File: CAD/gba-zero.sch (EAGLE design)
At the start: 57 parts, among them J1 SWTCHCRFT_3.5JACK5-JACK-SMD, P1 50_PIN_CON, P3 LINK_CONNECTOR, Q1 BSS138, U1 APX803, U2 NC7WZ16, U3 74LVC2G02, U4 74LVC3G04, U5 LM4875, U6 RPI-ZEROSMD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

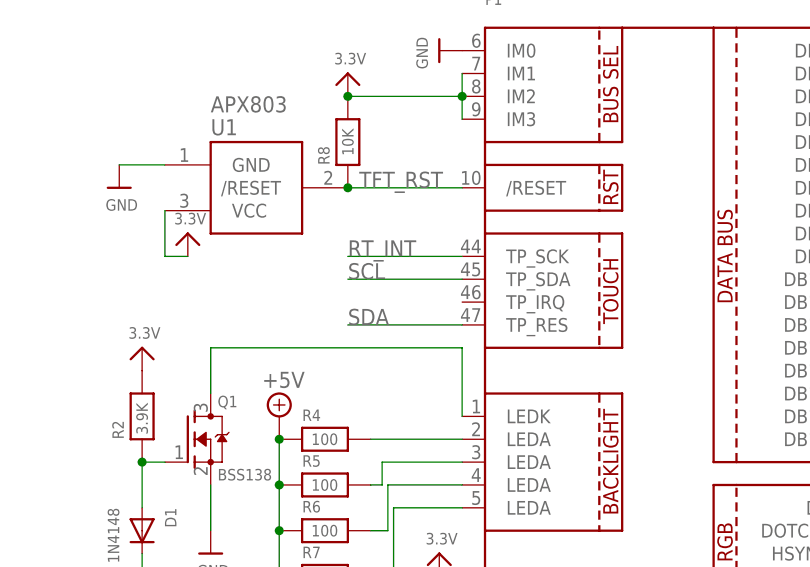
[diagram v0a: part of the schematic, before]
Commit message: Rerouted display control lines Added missing connection between pins 10 & 47 on the display connector
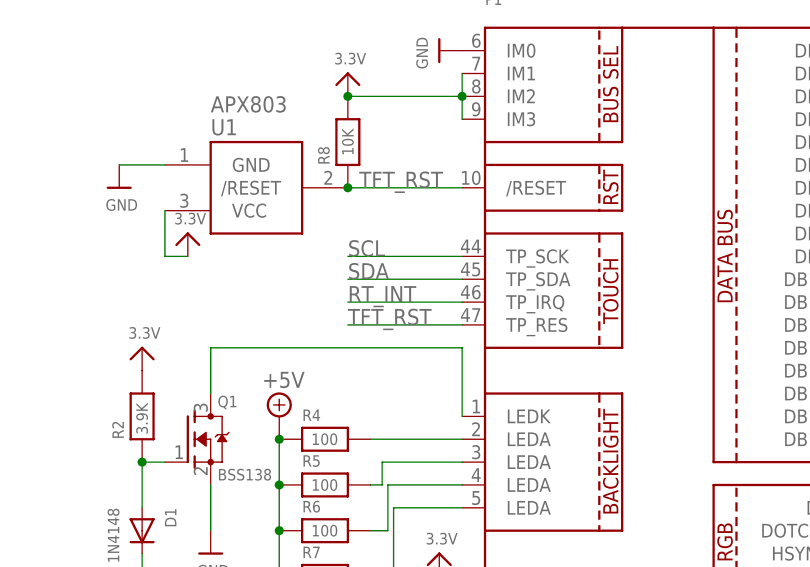
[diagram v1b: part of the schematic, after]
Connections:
- net RT_INT: now also P1.TP_IRQ; no longer P1.TP_SCK
- net SCL: now also P1.TP_SCK; no longer P1.TP_SDA
- net SDA: now also P1.TP_SDA; no longer P1.TP_RES
- net TFT_RST: now also P1.TP_RES
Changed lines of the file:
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@@
 <junction x="45.72" y="83.82"/>
+</segment>
+<segment>
+<wire x1="45.72" y1="68.58" x2="58.42" y2="68.58" width="0.1524" layer="91"/>
+<label x="45.72" y="68.58" size="1.778" layer="95"/>
+<pinref part="P1" gate="G$1" pin="TP_RES"/>
 </segment>
 </net>
@@
 </segment>
 <segment>
-<wire x1="58.42" y1="76.2" x2="45.72" y2="76.2" width="0.1524" layer="91"/>
-<pinref part="P1" gate="G$1" pin="TP_SCK"/>
-<label x="45.72" y="76.2" size="1.778" layer="95"/>
+<wire x1="58.42" y1="71.12" x2="45.72" y2="71.12" width="0.1524" layer="91"/>
+<label x="45.72" y="71.12" size="1.778" layer="95"/>
+<pinref part="P1" gate="G$1" pin="TP_IRQ"/>
 </segment>
 </net>
@@
 </segment>
 <segment>
-<pinref part="P1" gate="G$1" pin="TP_RES"/>
-<wire x1="58.42" y1="68.58" x2="45.72" y2="68.58" width="0.1524" layer="91"/>
-<label x="45.72" y="68.58" size="1.778" layer="95"/>
+<wire x1="58.42" y1="73.66" x2="45.72" y2="73.66" width="0.1524" layer="91"/>
+<label x="45.72" y="73.66" size="1.778" layer="95"/>
+<pinref part="P1" gate="G$1" pin="TP_SDA"/>
 </segment>
 </net>
@@
 </segment>
 <segment>
-<pinref part="P1" gate="G$1" pin="TP_SDA"/>
-<wire x1="58.42" y1="73.66" x2="45.72" y2="73.66" width="0.1524" layer="91"/>
-<label x="45.72" y="73.66" size="1.778" layer="95"/>
+<wire x1="58.42" y1="76.2" x2="45.72" y2="76.2" width="0.1524" layer="91"/>
+<label x="45.72" y="76.2" size="1.778" layer="95"/>
+<pinref part="P1" gate="G$1" pin="TP_SCK"/>
 </segment>
 </net>

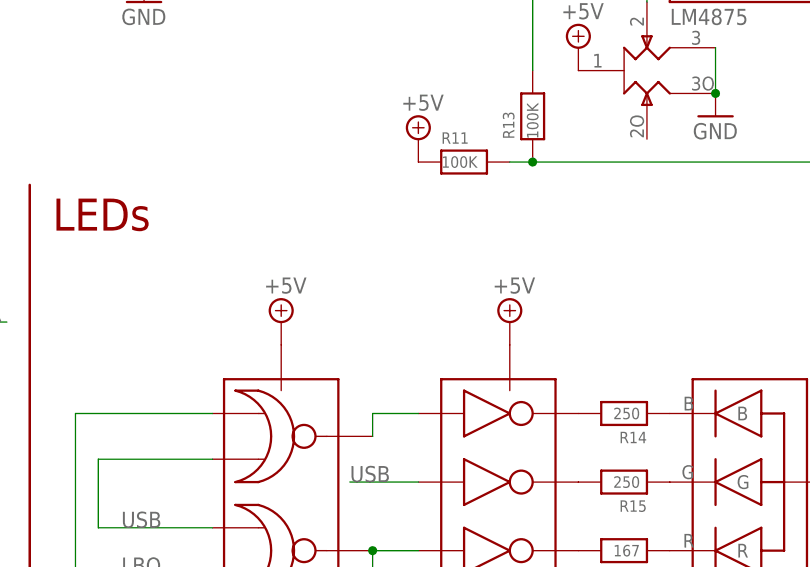
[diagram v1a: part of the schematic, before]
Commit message: Added diodes to power LED logic by USB & regulated 5V Cleaned up layout
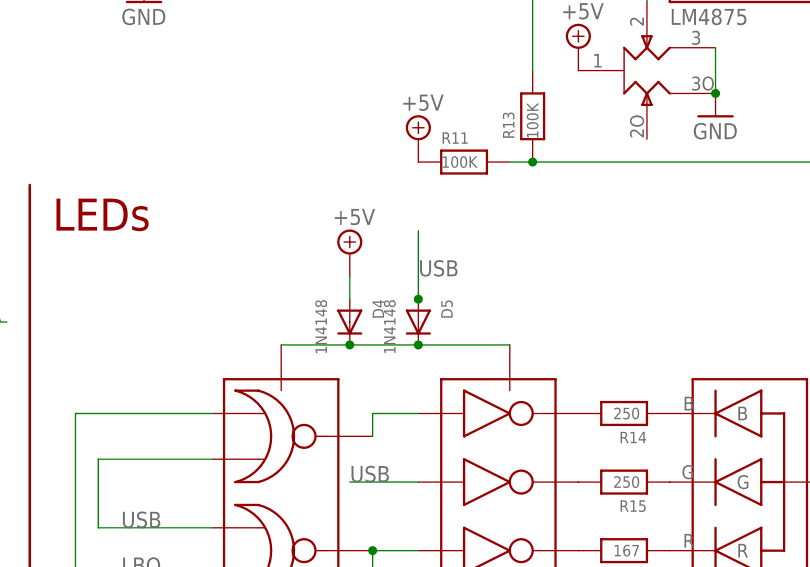
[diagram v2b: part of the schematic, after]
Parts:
- added D4, D5: 1N4148, microbuilder:DIODESOD-323
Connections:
- new net N$19: D4.C, D5.C, U3.VCC, U4.VCC
- net +5V: now also D4.A; no longer U3.VCC, U4.VCC
- net USB: now also D5.A
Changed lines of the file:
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@@
 <part name="D2" library="gba-zero-parts" deviceset="LTST-C19HE1WT" device=""/>
 <part name="SUPPLY2" library="supply2" deviceset="+5V" device=""/>
-<part name="SUPPLY5" library="supply2" deviceset="+5V" device=""/>
 <part name="SUPPLY9" library="supply2" deviceset="+5V" device=""/>
 <part name="GND7" library="microbuilder" deviceset="GND" device=""/>
@@
 <part name="R1" library="microbuilder" deviceset="RESISTOR" device="0603" value="0"/>
 <part name="R3" library="microbuilder" deviceset="RESISTOR" device="0603" value="0"/>
+<part name="D4" library="microbuilder" deviceset="DIODE" device="SOD-323" value="1N4148"/>
+<part name="D5" library="microbuilder" deviceset="DIODE" device="SOD-323" value="1N4148"/>
 </parts>
 <sheets>
@@
 <instance part="U4" gate="G$1" x="104.14" y="152.4"/>
 <instance part="D2" gate="G$1" x="129.54" y="152.4" rot="R180"/>
-<instance part="SUPPLY2" gate="+5V" x="78.74" y="170.18"/>
-<instance part="SUPPLY5" gate="+5V" x="104.14" y="170.18"/>
+<instance part="SUPPLY2" gate="+5V" x="86.36" y="177.8"/>
 <instance part="SUPPLY9" gate="+5V" x="139.7" y="154.94"/>
 <instance part="GND7" gate="G$1" x="78.74" y="132.08" rot="MR0"/>
@@
 <attribute name="VALUE" x="24.765" y="34.798" size="1.27" layer="96" font="vector" rot="R270"/>
 </instance>
+<instance part="D4" gate="G$1" x="86.36" y="170.18" rot="R270"/>
+<instance part="D5" gate="G$1" x="93.98" y="170.18" rot="R270"/>
 </instances>
 <busses>
@@
 <junction x="231.14" y="172.72"/>
 </segment>
+<segment>
+<wire x1="93.98" y1="172.72" x2="93.98" y2="180.34" width="0.1524" layer="91"/>
+<label x="93.98" y="175.26" size="1.778" layer="95"/>
+<pinref part="D5" gate="G$1" pin="A"/>
+<junction x="93.98" y="172.72"/>
+</segment>
 </net>
 <net name="LBO" class="0">
@@
 </segment>
 <segment>
-<pinref part="U3" gate="G$1" pin="VCC"/>
-<pinref part="SUPPLY2" gate="+5V" pin="+5V"/>
-</segment>
-<segment>
-<pinref part="U4" gate="G$1" pin="VCC"/>
-<pinref part="SUPPLY5" gate="+5V" pin="+5V"/>
-</segment>
-<segment>
 <pinref part="D2" gate="G$1" pin="VCC"/>
 <pinref part="SUPPLY9" gate="+5V" pin="+5V"/>
@@
 <pinref part="C9" gate="G$1" pin="P$1"/>
 <pinref part="SUPPLY8" gate="+5V" pin="+5V"/>
+</segment>
+<segment>
+<pinref part="D4" gate="G$1" pin="A"/>
+<pinref part="SUPPLY2" gate="+5V" pin="+5V"/>
+<wire x1="86.36" y1="175.26" x2="86.36" y2="172.72" width="0.1524" layer="91"/>
 </segment>
 </net>
@@
 </segment>
 </net>
+<net name="N$19" class="0">
+<segment>
+<pinref part="U3" gate="G$1" pin="VCC"/>
+<pinref part="U4" gate="G$1" pin="VCC"/>
+<wire x1="78.74" y1="167.64" x2="86.36" y2="167.64" width="0.1524" layer="91"/>
+<pinref part="D4" gate="G$1" pin="C"/>
+<wire x1="86.36" y1="167.64" x2="93.98" y2="167.64" width="0.1524" layer="91"/>
+<junction x="86.36" y="167.64"/>
+<pinref part="D5" gate="G$1" pin="C"/>
+<wire x1="93.98" y1="167.64" x2="104.14" y2="167.64" width="0.1524" layer="91"/>
+<junction x="93.98" y="167.64"/>
+</segment>
+</net>

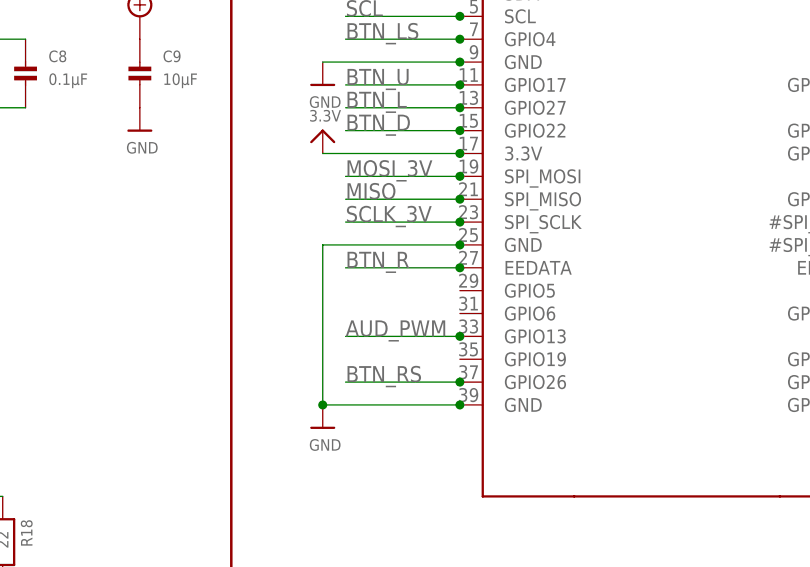
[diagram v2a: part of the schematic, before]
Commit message: Added LBO to a GPIO5
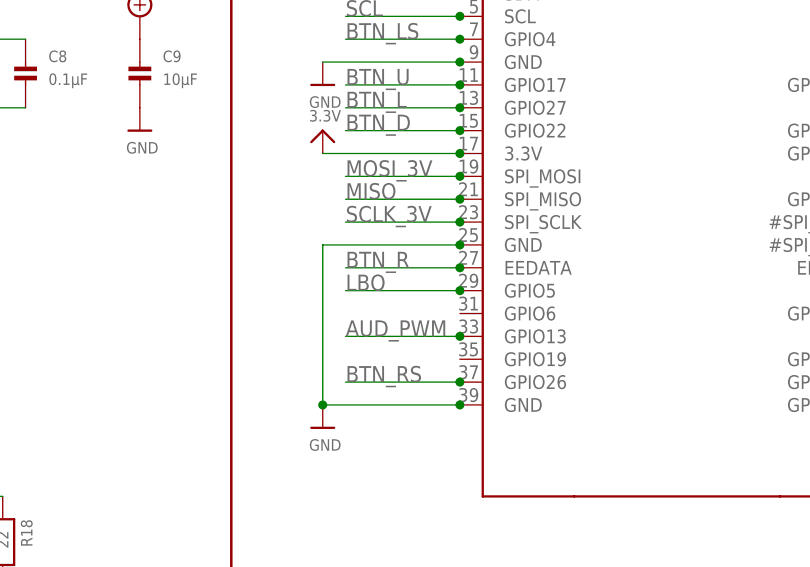
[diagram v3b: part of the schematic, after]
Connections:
- net LBO: now also U6.GPIO5
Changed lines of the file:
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@@
 <pinref part="U7" gate="G$1" pin="LBO"/>
+</segment>
+<segment>
+<wire x1="160.02" y1="60.96" x2="172.72" y2="60.96" width="0.1524" layer="91"/>
+<pinref part="U6" gate="G$1" pin="GPIO5"/>
+<junction x="172.72" y="60.96"/>
+<label x="160.02" y="60.96" size="1.778" layer="95"/>
 </segment>
 </net>

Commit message: Replaced 0805s with 0603s Fattened power traces
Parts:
- C11, C12, C14: device microbuilder:CAP_CERAMIC0805 -> microbuilder:CAP_CERAMIC0603
- R14, R15, R16, R18, R19, R2, R4, R5, R6, R7, R8: device microbuilder:RESISTOR0805 -> microbuilder:RESISTOR0603

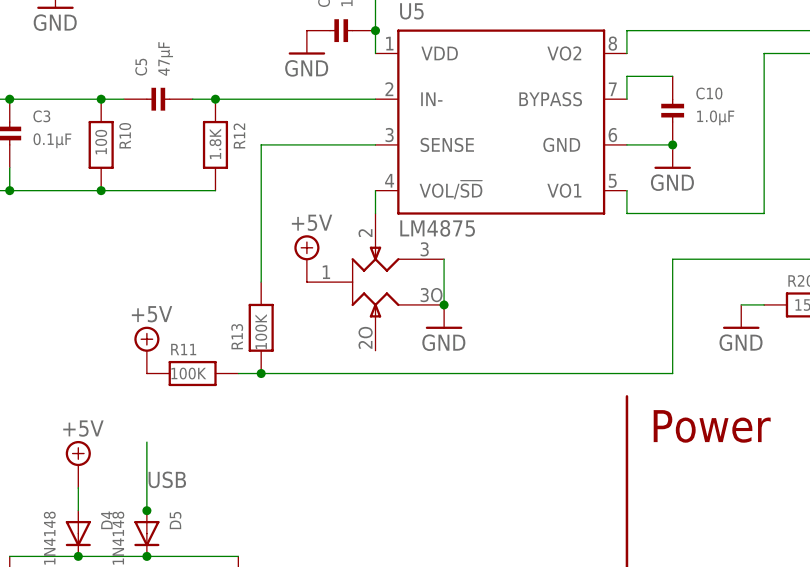
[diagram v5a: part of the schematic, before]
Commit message: Swapped VCC & GND for the volume dial
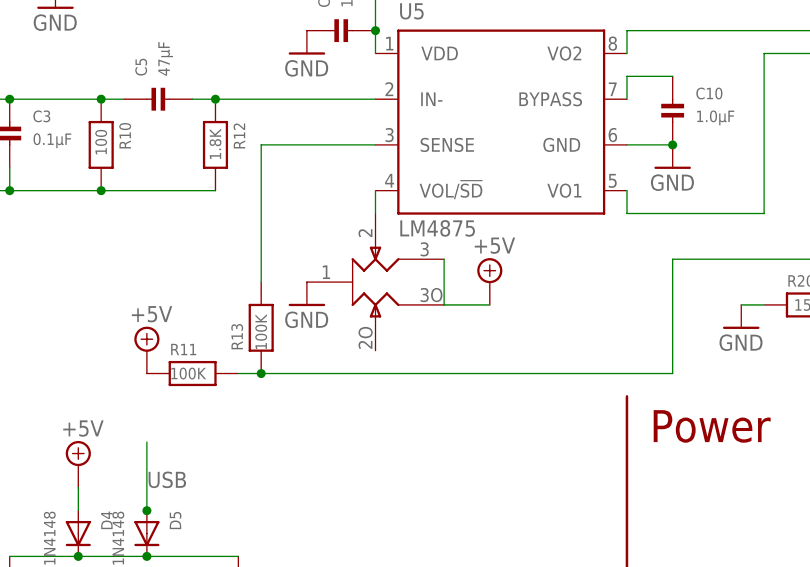
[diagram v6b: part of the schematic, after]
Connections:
- net +5V: now also R17.3, R17.3O; no longer R17.1
- net GND: now also R17.1; no longer R17.3, R17.3O
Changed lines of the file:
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@@
 <attribute name="VALUE" x="187.96" y="227.33" size="1.27" layer="96"/>
 </instance>
-<instance part="GND12" gate="1" x="127" y="193.04"/>
+<instance part="GND12" gate="1" x="111.76" y="195.58"/>
 <instance part="GND10" gate="1" x="111.76" y="223.52"/>
 <instance part="GND8" gate="1" x="83.82" y="228.6"/>
@@
 <instance part="SUPPLY7" gate="+5V" x="119.38" y="233.68"/>
 <instance part="SUPPLY3" gate="+5V" x="83.82" y="241.3"/>
-<instance part="SUPPLY6" gate="+5V" x="111.76" y="200.66"/>
+<instance part="SUPPLY6" gate="+5V" x="132.08" y="198.12"/>
 <instance part="VCC5" gate="G$1" x="63.5" y="218.44"/>
 <instance part="GND6" gate="1" x="63.5" y="205.74"/>
@@
 </segment>
 <segment>
-<pinref part="R17" gate="G$1" pin="3"/>
-<pinref part="R17" gate="G$1" pin="3O"/>
-<wire x1="127" y1="200.66" x2="127" y2="195.58" width="0.1524" layer="91"/>
-<pinref part="GND12" gate="1" pin="GND"/>
-<junction x="127" y="195.58"/>
-</segment>
-<segment>
 <pinref part="C10" gate="G$1" pin="P$2"/>
 <pinref part="GND14" gate="1" pin="GND"/>
@@
 <wire x1="119.38" y1="81.28" x2="124.46" y2="81.28" width="0.1524" layer="91"/>
 <junction x="119.38" y="81.28"/>
+</segment>
+<segment>
+<pinref part="R17" gate="G$1" pin="1"/>
+<pinref part="GND12" gate="1" pin="GND"/>
 </segment>
 </net>
@@
 </segment>
 <segment>
-<pinref part="R17" gate="G$1" pin="1"/>
-<pinref part="SUPPLY6" gate="+5V" pin="+5V"/>
-</segment>
-<segment>
 <pinref part="U7" gate="G$1" pin="5V"/>
 <pinref part="SUPPLY11" gate="+5V" pin="+5V"/>
@@
 <wire x1="86.36" y1="175.26" x2="86.36" y2="172.72" width="0.1524" layer="91"/>
 </segment>
-</net>
+<segment>
+<pinref part="R17" gate="G$1" pin="3"/>
+<pinref part="R17" gate="G$1" pin="3O"/>
+<wire x1="127" y1="200.66" x2="127" y2="195.58" width="0.1524" layer="91"/>
+<pinref part="SUPPLY6" gate="+5V" pin="+5V"/>
+<wire x1="127" y1="195.58" x2="132.08" y2="195.58" width="0.1524" layer="91"/>
+</segment>
+</net>

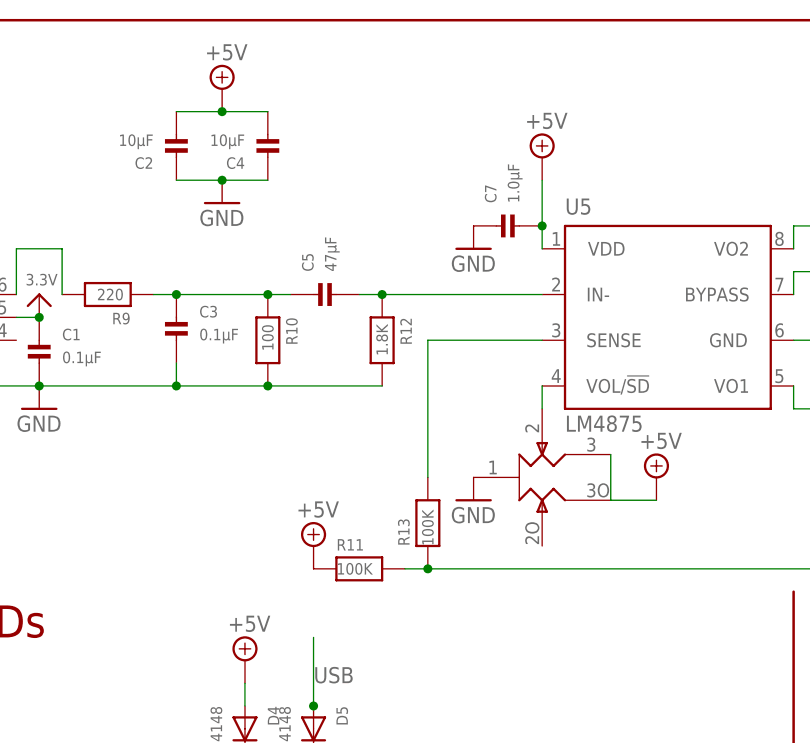
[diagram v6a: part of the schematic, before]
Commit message: Cleaned up the silkscreen
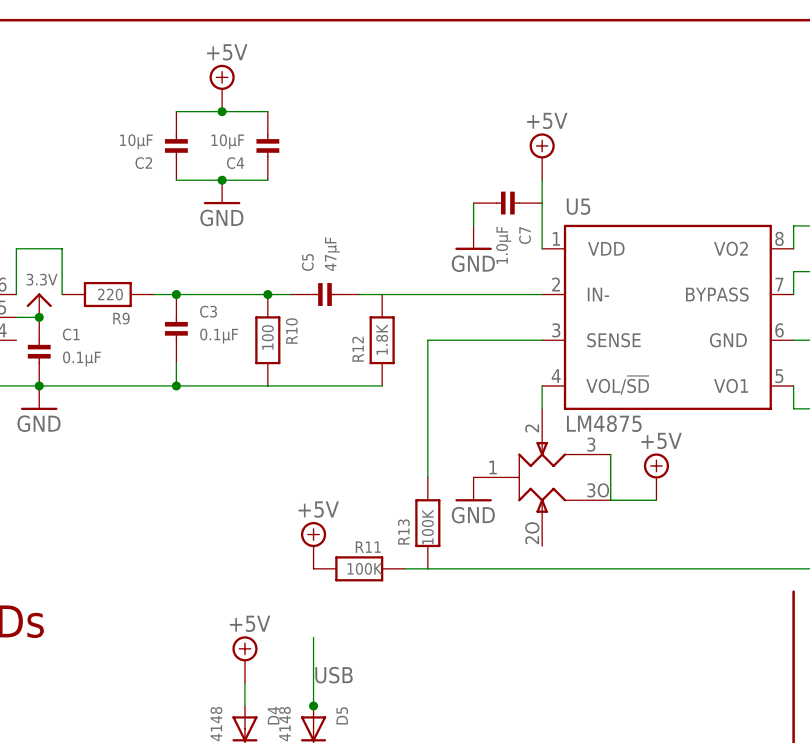
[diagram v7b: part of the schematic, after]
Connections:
- removed net IN-: C5.P$2, R12.1, U5.IN-
- new net N$23: C5.P$2, R12.2, U5.IN-
- net +5V: now also C7.P$1, R11.2; no longer C7.P$2, R11.1
- net GND: now also C7.P$2, R12.1; no longer C7.P$1, R12.2
- net N$22: now also R11.1; no longer R11.2
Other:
- moved on the sheet: C7, R11, R12
